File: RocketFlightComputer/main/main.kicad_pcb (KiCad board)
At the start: 4 copper layers, 53.7 x 53.7 mm, 123 parts, among them Q1 DMG3406L, Q2 SI2302, Q3 SI2302, Y1 32.768kHz, Y3 32.768kHz, Y4 32.768kHz, Y5 XRCGB24M000F2P29R0

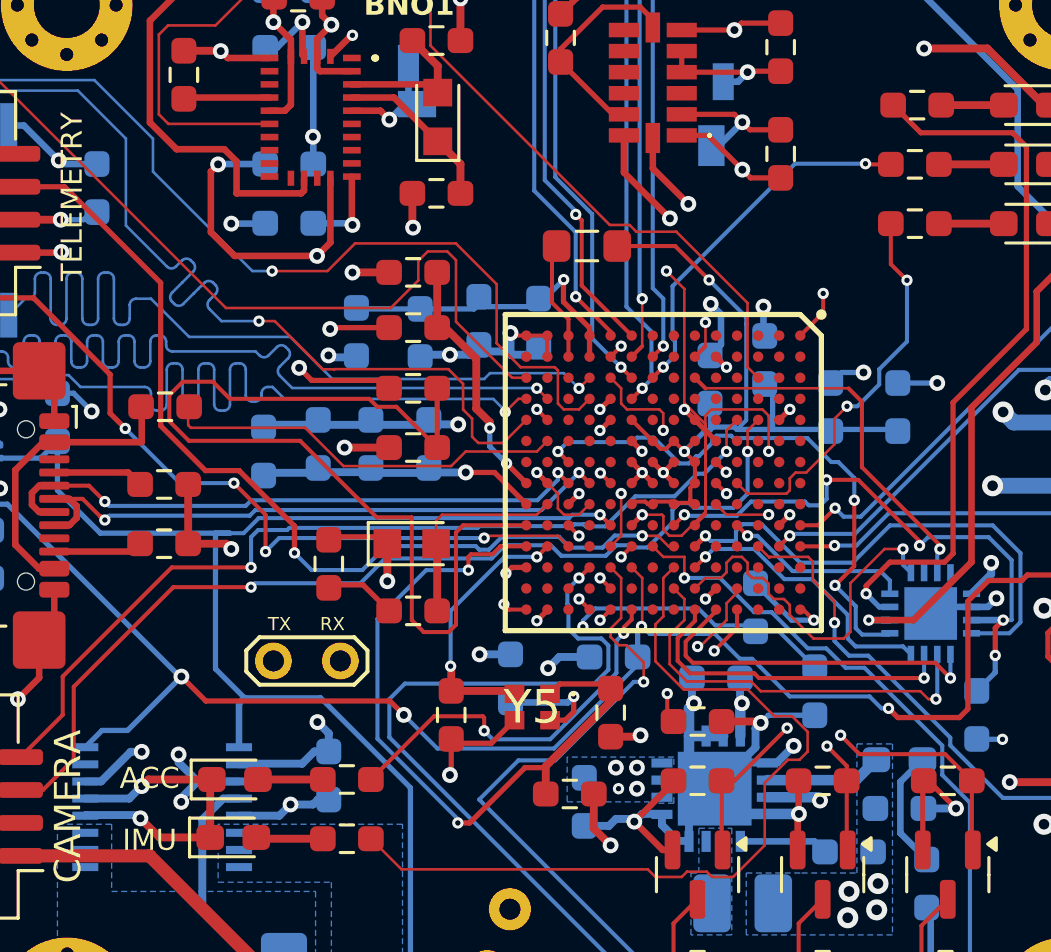
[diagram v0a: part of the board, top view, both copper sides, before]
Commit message: Corrections of mistake, revision of schematic is done and BOM revised, revision of pcb layout to do
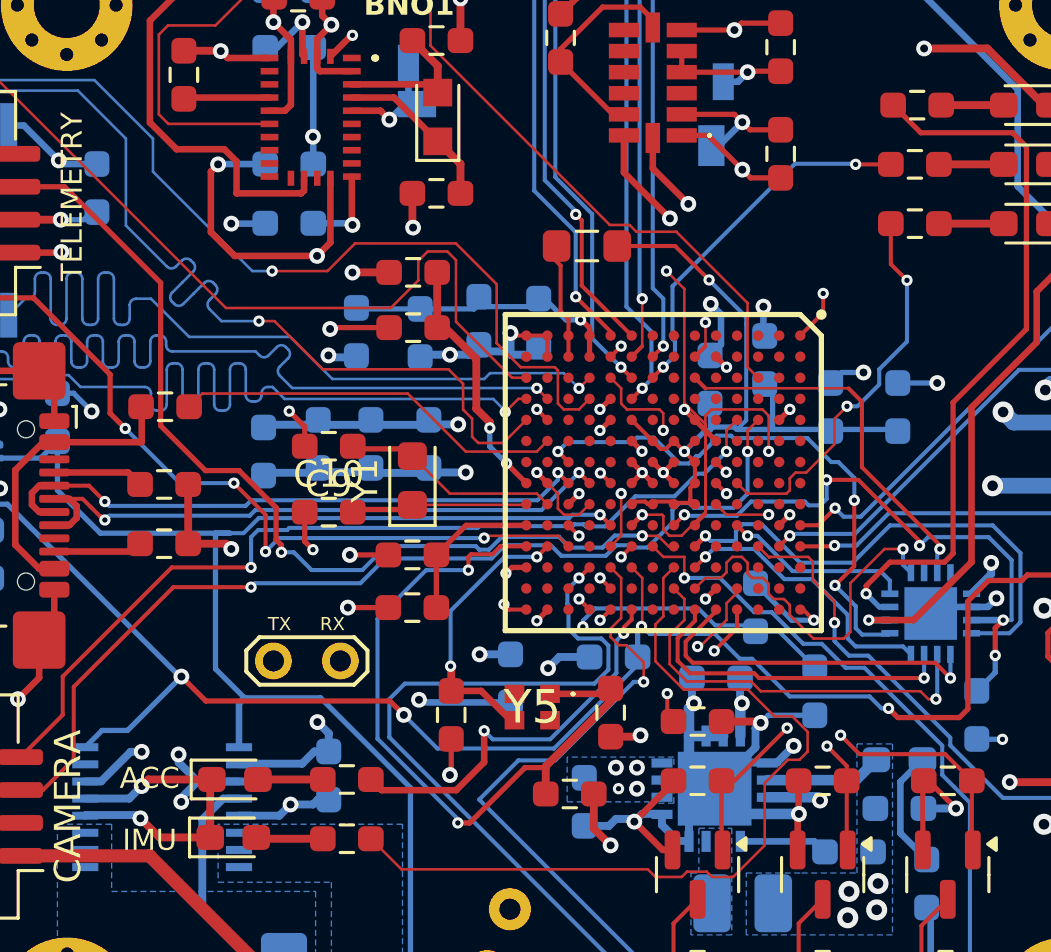
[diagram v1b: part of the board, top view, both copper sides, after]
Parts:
- C17: value 0.22uF -> 10nf
- C7: value 10nF -> 10uF
- R4: value 1k -> 470
- moved C16 8.33 mm to (104.1, 62.5)
- moved C9 7.02 mm to (100.9, 56.3)
- moved C21 4.08 mm to (104.1, 60.5)
- moved Y1 2.40 mm to (104.1, 57.6), turned to 90 degrees
- moved C10 1.96 mm to (100.9, 58.8), turned to 0 degrees
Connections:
- net /3.3v_led renamed Net-(D1-K)
- C10 pad 1: Net-(C10-Pad1) -> GNDREF
- C10 pad 2: GNDREF -> Net-(MIMXRT1062DVL6B1-RTC_XTALO)
- C9 pad 2: Net-(C10-Pad1) -> GNDREF
- MIMXRT1062DVL6B1 pad P9: GNDREF -> Net-(MIMXRT1062DVL6B1-RTC_XTALO)
- Y1 pad 1: GNDREF -> Net-(MIMXRT1062DVL6B1-RTC_XTALO)
- Y5 pad 2: /N11 -> unconnected-(Y5-NC_1-Pad2)
- Y5 pad 3: GNDREF -> /N11
- Y5 pad 4: GNDREF -> unconnected-(Y5-NC_2-Pad4)
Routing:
- net Net-(MIMXRT1062DVL6B1-NVCC_PLL): track 37.5 -> 5.88 mm
- net GNDREF: track 238.9 -> 230.6 mm, vias 132 -> 133
- net Net-(MIMXRT1062DVL6B1-RTC_XTALO): track 0.00 -> 6.71 mm
- net Net-(C10-Pad1): track 2.70 -> 0.00 mm
- net Net-(MIMXRT1062DVL6B1-DCDC_IN_1): track 11.0 -> 9.94 mm
- net /N11: track 10.0 -> 10.6 mm

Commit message: Because i am lazy i would call this the V1 of the avionics
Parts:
- R13: moved to F.Cu
- moved R13 0.72 mm to (126.2, 66.4)
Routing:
- net /P11: track 28.7 -> 20.9 mm, vias 2 -> 0
- net Net-(MKL02Z32VFG1-PTB3/IRQ_10): track 27.5 -> 23.2 mm
- net Net-(KMR241GLFS1-COM_1): track 32.0 -> 28.4 mm
- net /PTA3: track 30.5 -> 29.0 mm, vias 6 -> 5
- net /PTB1: track 21.4 -> 20.4 mm
- net +3.3V: track 109.6 -> 108.9 mm
- net Net-(MIMXRT1062DVL6B1-GPIO_B0_03): track 14.9 -> 14.3 mm
- net Net-(FB1-Pad1): track 10.8 -> 10.2 mm
- net Net-(MIMXRT1062DVL6B1-RTC_XTALI): track 8.30 -> 7.77 mm
- net /N11: track 10.6 -> 10.4 mm, vias 2 -> 0
- net GNDREF: vias 133 -> 134

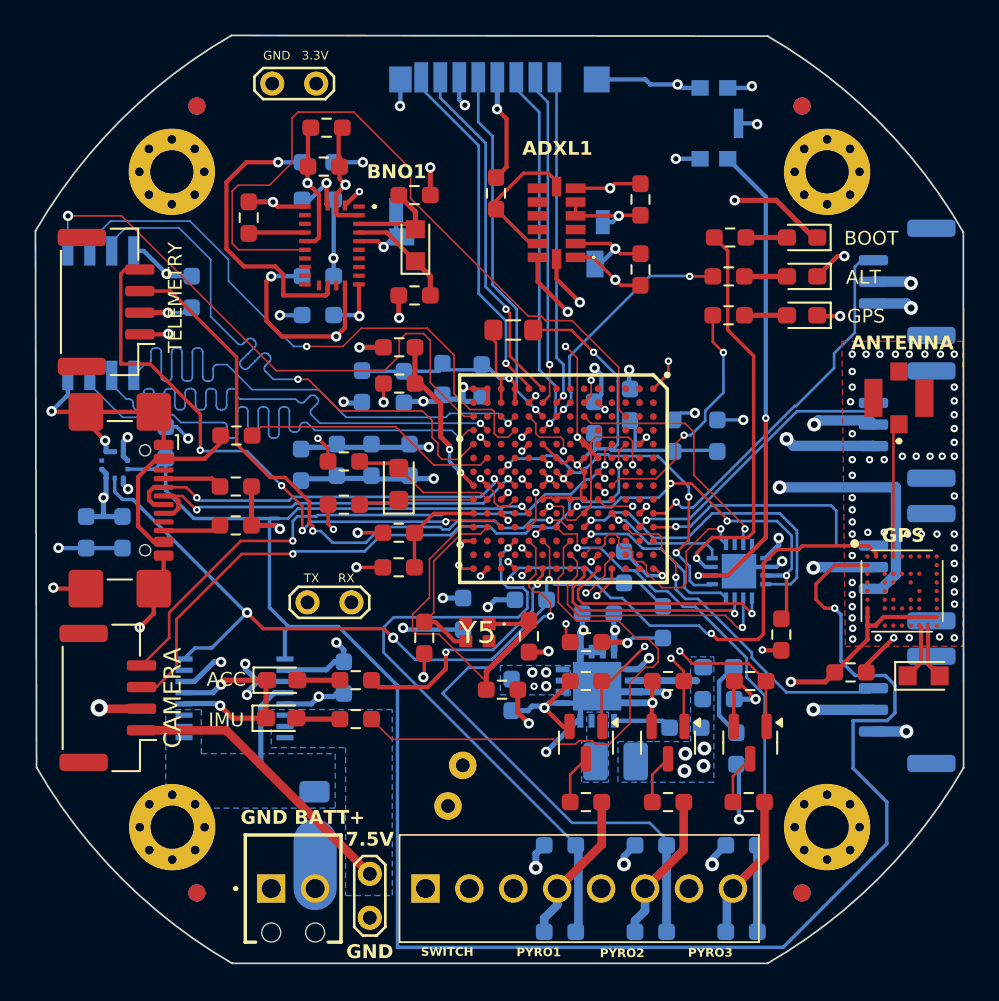
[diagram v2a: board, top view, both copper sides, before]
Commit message: Was missing pull ups on adxl375
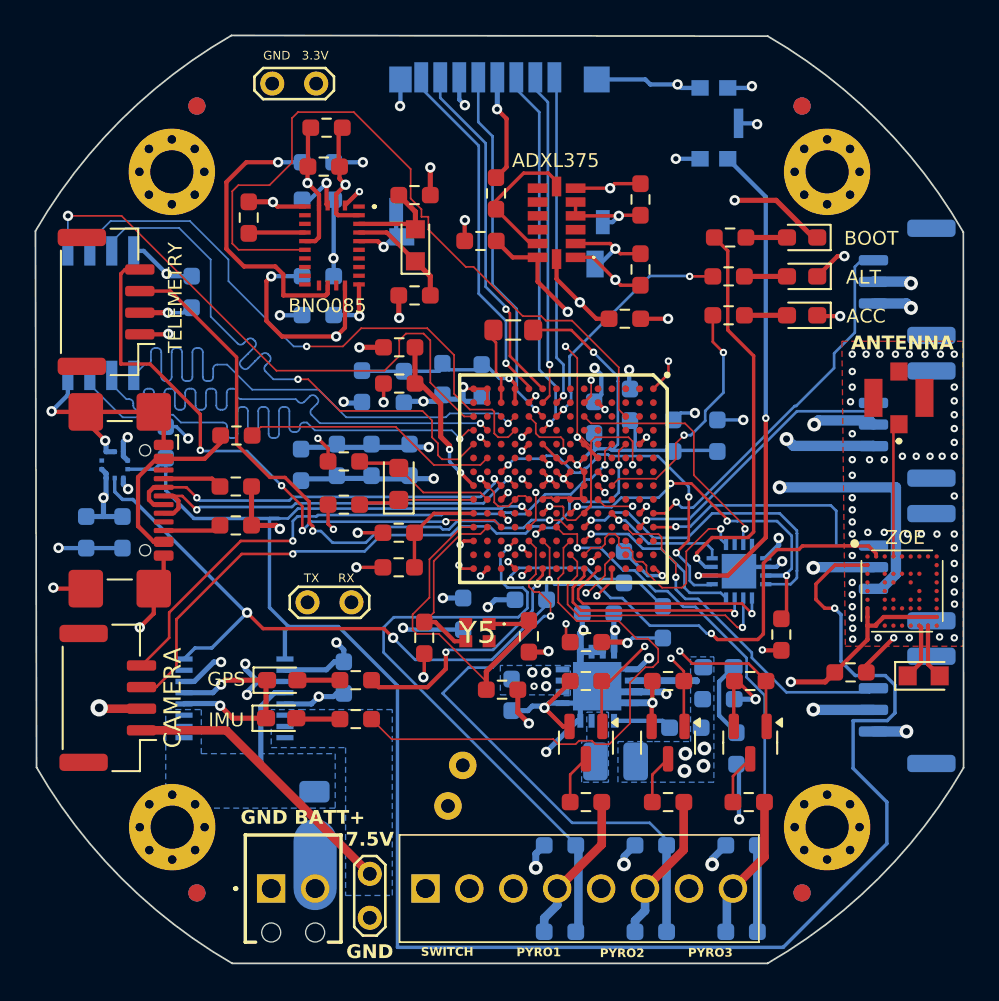
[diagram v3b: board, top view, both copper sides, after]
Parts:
- added R18: 4.7k, Resistor_SMD:R_0603_1608Metric_Pad0.98x0.95mm_HandSolder, F.Cu at (108.8, 43.6)
- added R32: 4.7k, Resistor_SMD:R_0603_1608Metric_Pad0.98x0.95mm_HandSolder, F.Cu at (117.1, 48.1)
- C17: value 10nf -> 10nF
- Q2, Q3: value SI2302 -> DMG3406L
- R23, R27, R31: value 7k -> 7.32k
- R30: value 7k -> 10k
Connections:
- MIMXRT1062DVL6B1 pad K9: unconnected-(MIMXRT1062DVL6B1-NGND_KEL0-PadK9) -> GNDREF
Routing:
- net +3.3V: track 108.9 -> 111.7 mm, vias 34 -> 36
- net /ADXL375_SDA2: track 24.7 -> 27.5 mm
- net /ADXL375_SCL2: track 22.6 -> 24.6 mm
- net GNDREF: track 230.6 -> 231.5 mm
- net /BNO085_RST: track 43.2 -> 43.9 mm
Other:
- board text added: "ADXL375"
- board text added: "BNO085"
- board text added: "FLASH"
- board text added: "INA260"
- board text added: "ZOE"

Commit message: REVA board?
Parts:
- renumbered S4B-PH-K-S_LF__SN_1 to JST-GH-1, S4B-PH-K-S_LF__SN_2 to JST-GH-2
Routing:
- net +3.3V: track 111.7 -> 102.3 mm, vias 36 -> 35
- net /Pyro2_Test_41: track 34.9 -> 31.7 mm
- net GNDREF: track 231.5 -> 229.1 mm
- net /Cam_RX: track 37.7 -> 35.7 mm
- net /BMP390_SCL1: track 114.0 -> 112.3 mm
- net /Reserve_RX: track 17.5 -> 16.5 mm
- net /Cam_TX: track 34.6 -> 33.7 mm
- net /Reserve_TX: track 20.5 -> 19.7 mm
- net Net-(MIMXRT1062DVL6B1-GPIO_B0_03): track 14.3 -> 13.5 mm

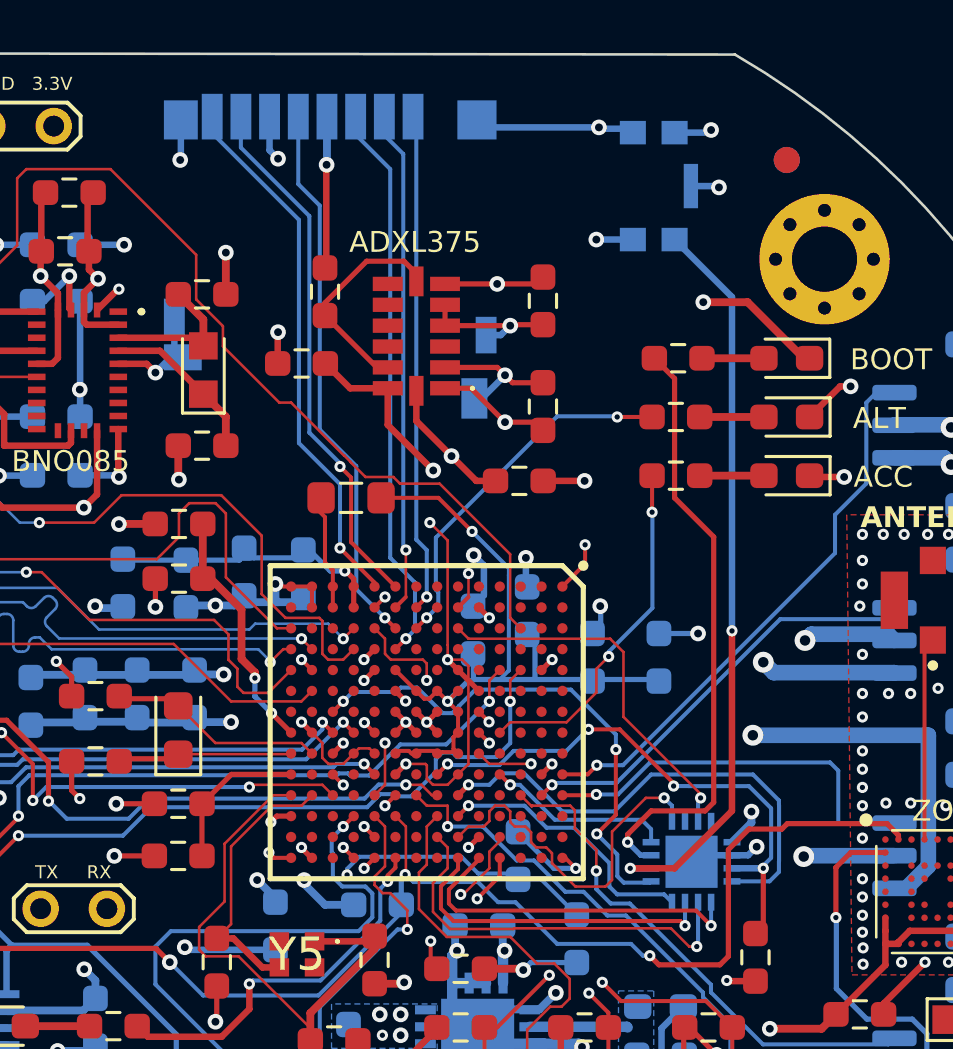
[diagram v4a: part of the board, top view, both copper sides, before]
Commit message: Addition of logos silkscreen
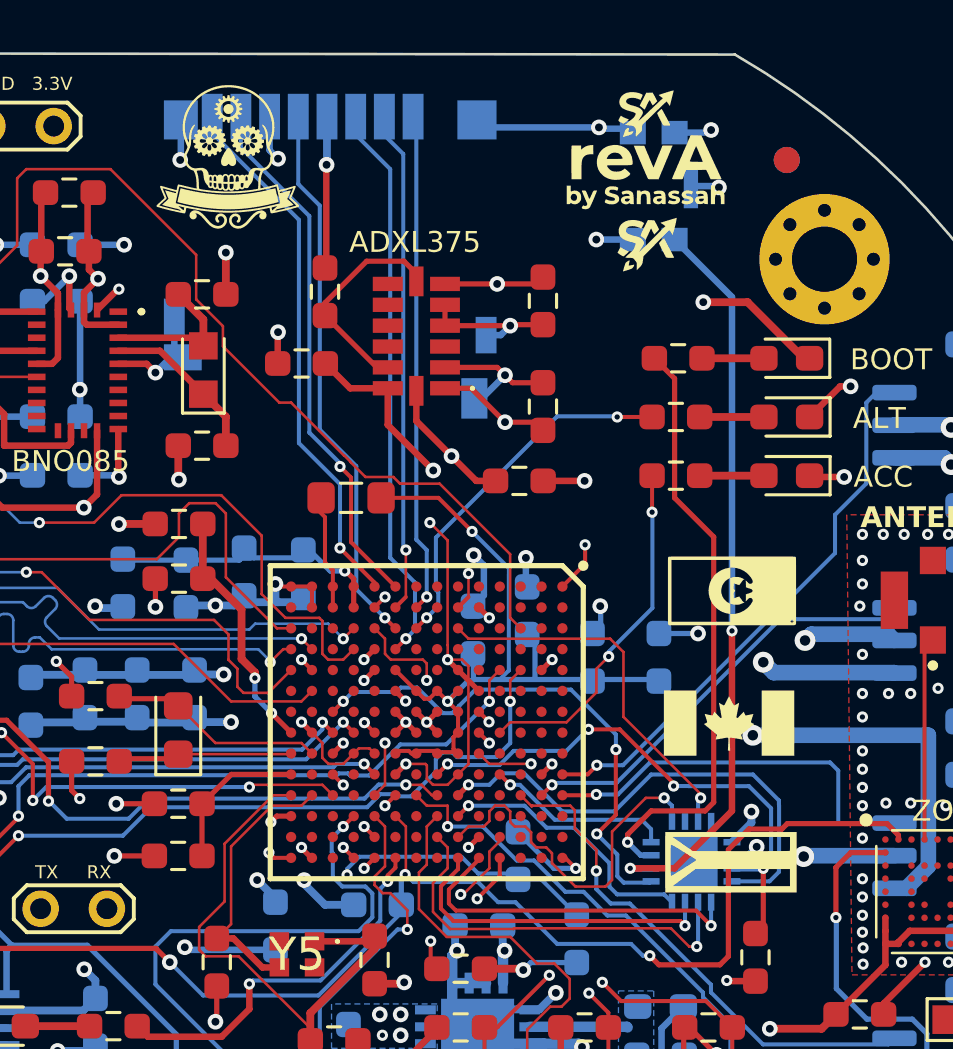
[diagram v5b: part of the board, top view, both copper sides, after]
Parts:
- added G***: LOGO, LOGO, F.Cu at (125.3, 52.3)
- added G***: LOGO, LOGO, F.Cu at (125.3, 62.7)
- added G***: LOGO, LOGO, F.Cu at (106.0, 35.7)
- added G***: LOGO, LOGO, F.Cu at (125.2, 57.4)
- added G***: LOGO, LOGO, F.Cu at (122.0, 36.5)
- added G***: LOGO, LOGO, B.Cu at (124.2, 46.6)
